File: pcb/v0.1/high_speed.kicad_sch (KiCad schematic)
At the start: 14 parts, among them J4 USB_C_Receptacle_fw, J5 USB_C_Receptacle_fw, J6 690-019-298-412, J7 Conn_01x22_Female, U2 AP22653W6, U3 RT9742SNGV

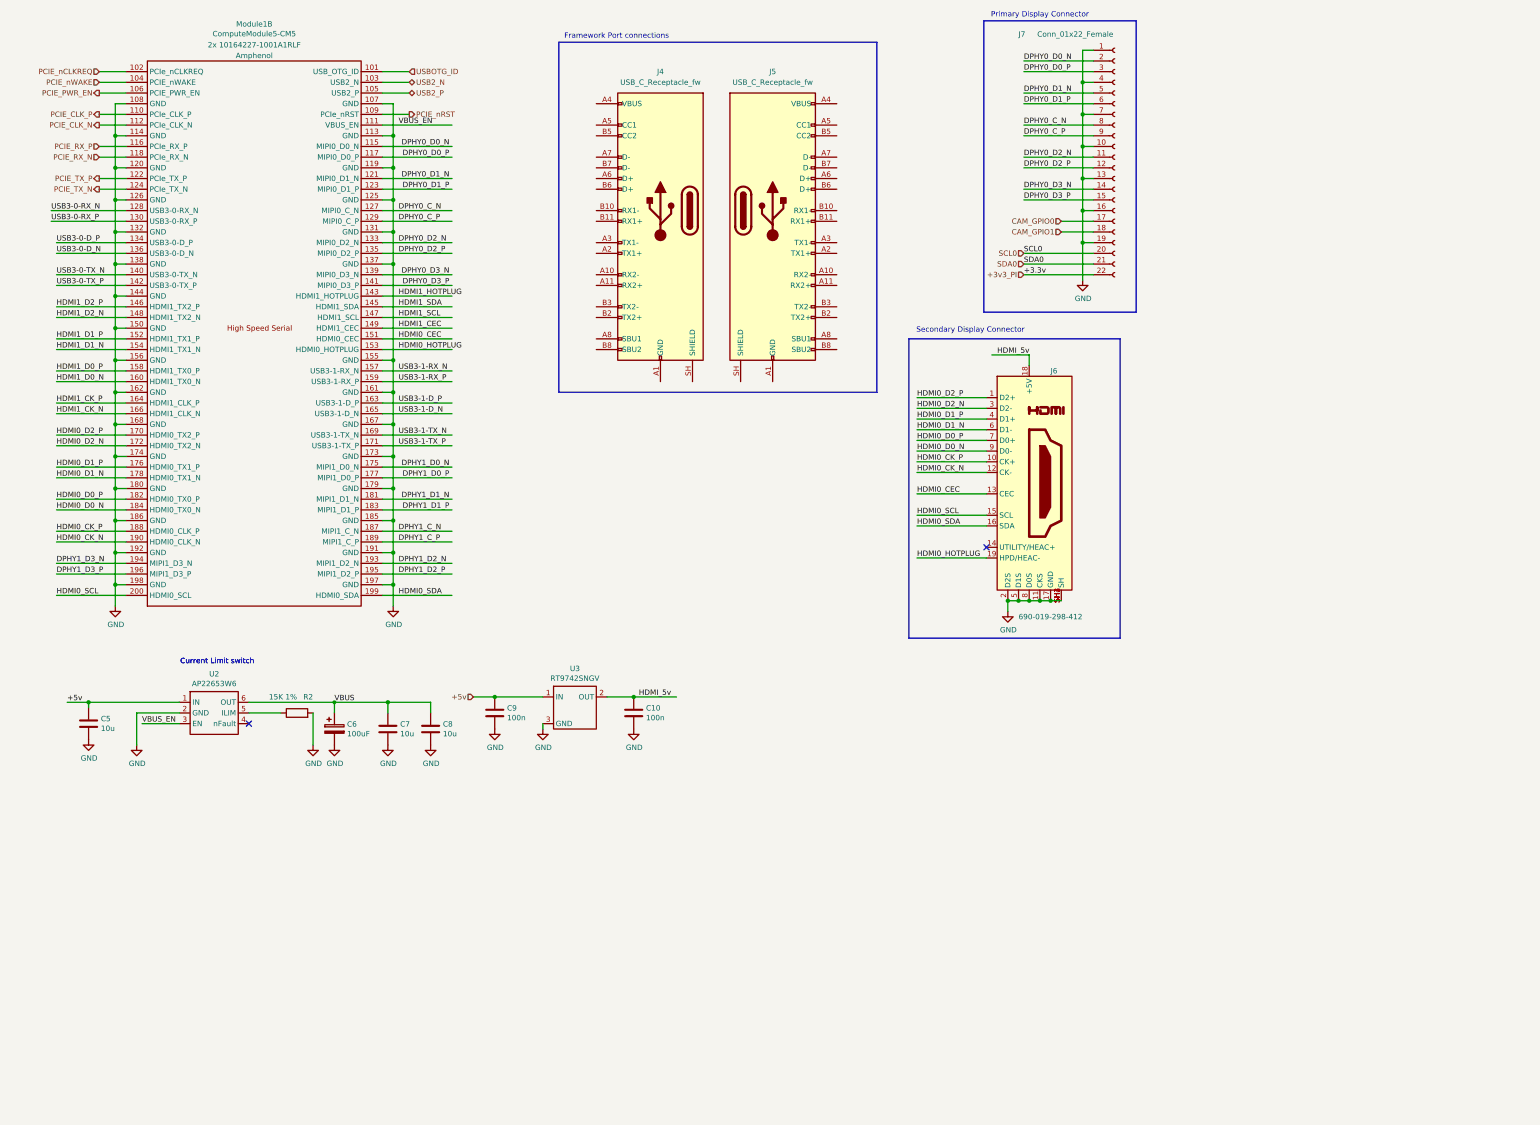
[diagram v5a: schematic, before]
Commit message: Base setup for FW usb ports
The USB system is not complete yet, but all of the basics are done. The
current limit switch, its capacitors, and usb connector parts are
sorted.

However, the current limit, CC pins and second port are not configured
yet.
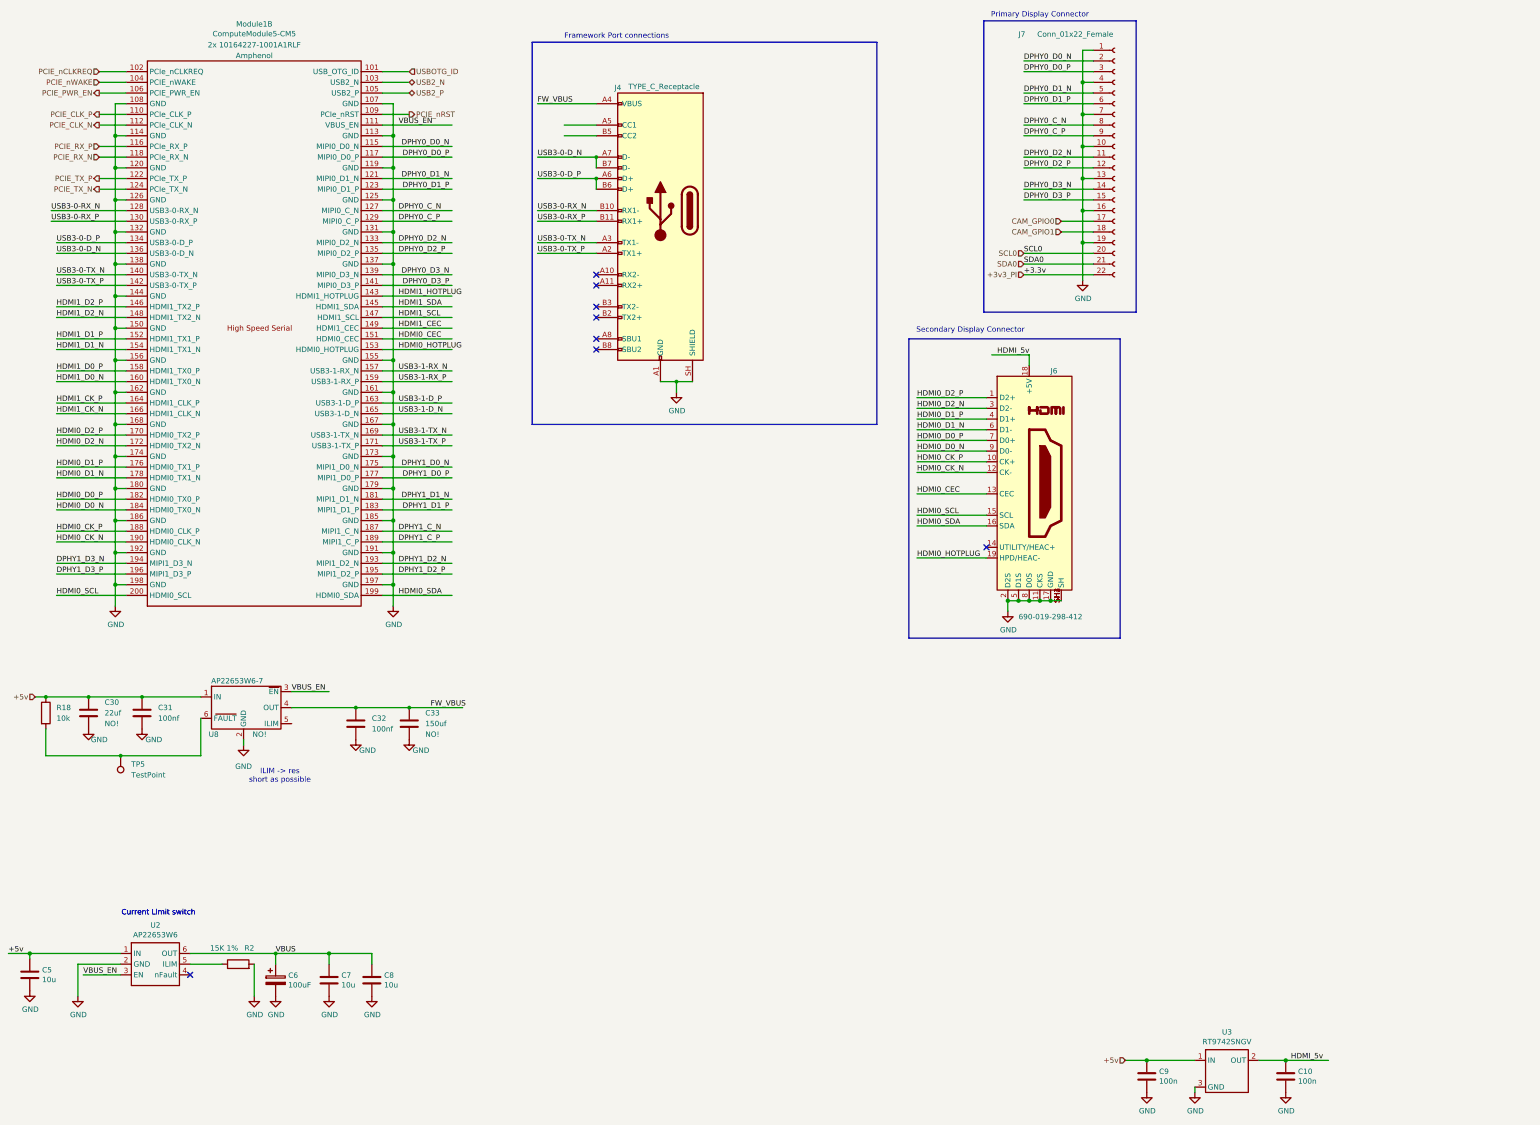
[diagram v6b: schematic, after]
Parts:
- removed J4, J5: USB_C_Receptacle_fw, symbol TH-1-CC:USB_C_Receptacle_fw
- added C30: 22uf, symbol TH-1-CC:C_22uf_AP
- added C31, C32: 100nf, Capacitor_SMD:C_0603_1608Metric, symbol TH-1-CC:C_100nf
- added C33: 150uf, symbol TH-1-CC:C_150uf_AP
- added J4: TYPE_C_Receptacle, symbol TH-1-CC:TYPE_C_Receptacle
- added R18: 10k, Resistor_SMD:R_0603_1608Metric, symbol TH-1-CC:R_10k
- added TP5: TestPoint, symbol Connector:TestPoint
- added U8: AP22653W6-7, symbol TH-1-CC:AP22653W6-7
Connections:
- net +5v: now also C30.1, C31.1, R18.1, U8.1 (IN)
- net GND: now also C30.2, C31.2, C32.2, C33.2, J4.A1 (GND), J4.A12 (GND), J4.B1 (GND), J4.B12 (GND), J4.SH (SHIELD), U8.2 (GND)
- net USB3-0-D_N: now also J4.A7 (D-), J4.B7 (D-)
- net USB3-0-D_P: now also J4.A6 (D+), J4.B6 (D+)
- net USB3-0-RX_N: now also J4.B10 (RX1-)
- net USB3-0-RX_P: now also J4.B11 (RX1+)
- net USB3-0-TX_N: now also J4.A3 (TX1-)
- net USB3-0-TX_P: now also J4.A2 (TX1+)
- net VBUS_EN: now also U8.3 (EN)
- new net: R18.2, TP5.1, U8.6 (FAULT)
- new net FW_VBUS: C32.1, C33.1, J4.A4 (VBUS), J4.A9 (VBUS), J4.B4 (VBUS), J4.B9 (VBUS), U8.4 (OUT)
- no-connect marks 2 -> 8
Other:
- note added: "ILIM -> res short as possible"
- moved on the sheet: C10, C5, C6, C7, C8, C9, R2, U2, U3

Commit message: Finish USB ports!!!
Theoretically both the power input usb type-c port and the two host side
ports are complete. Including a current limit IC that caps the two host
ports at a combined 1.2A.

ESD protection is probably still needed!!!
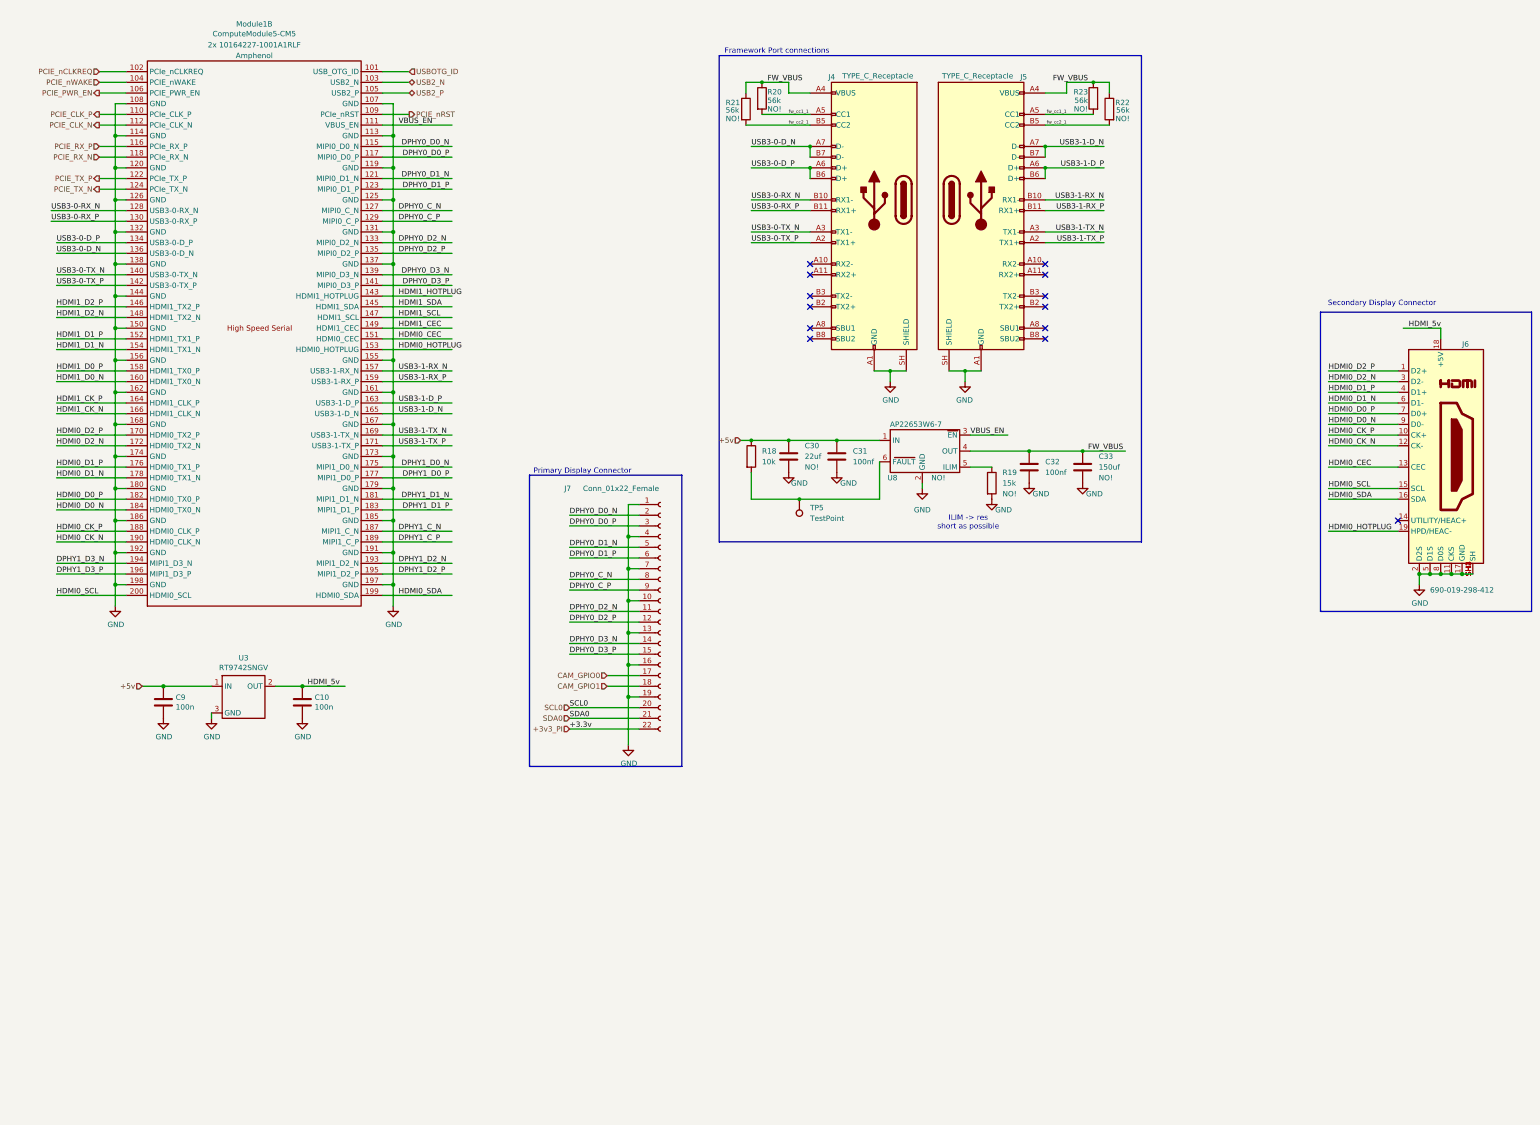
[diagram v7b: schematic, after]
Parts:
- removed C5, C7, C8: 10u, Capacitor_SMD:C_0805_2012Metric, symbol Device:C
- removed C6: 100uF, Capacitor_Tantalum_SMD:CP_EIA-7343-31_Kemet-D, symbol Device:C_Polarized
- removed R2: 15K 1%, Resistor_SMD:R_0402_1005Metric, symbol Device:R
- removed U2: AP22653W6, Package_TO_SOT_SMD:SOT-23-6, symbol CM5IO:AP2553W6
- added J5: TYPE_C_Receptacle, symbol TH-1-CC:TYPE_C_Receptacle
- added R19: 15k, Resistor_SMD:R_0603_1608Metric, symbol TH-1-CC:R_15k
- added R20, R21, R22, R23: 56k, Resistor_SMD:R_0603_1608Metric, symbol TH-1-CC:R_56k
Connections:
- net FW_VBUS: now also J5.A4 (VBUS), J5.A9 (VBUS), J5.B4 (VBUS), J5.B9 (VBUS), R20.1, R21.1, R22.1, R23.1
- net GND: now also J5.A1 (GND), J5.A12 (GND), J5.B1 (GND), J5.B12 (GND), J5.SH (SHIELD), R19.2
- net USB3-1-D_N: now also J5.A7 (D-), J5.B7 (D-)
- net USB3-1-D_P: now also J5.A6 (D+), J5.B6 (D+)
- net USB3-1-RX_N: now also J5.B10 (RX1-)
- net USB3-1-RX_P: now also J5.B11 (RX1+)
- net USB3-1-TX_N: now also J5.A3 (TX1-)
- net USB3-1-TX_P: now also J5.A2 (TX1+)
- net fw_cc1_1: now reaches J4.A5 (CC1)
- net fw_cc1_1: now also J5.A5 (CC1), R20.2, R23.2
- net fw_cc2_1: now reaches J4.B5 (CC2)
- net fw_cc2_1: now also J5.B5 (CC2), R21.2, R22.2
- net at U8.5 (ILIM): now also R19.1
- no-connect marks 8 -> 13
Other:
- note removed: "Current Limit switch"
- moved on the sheet: C10, C30, C31, C32, C33, C9, J4, J6, J7, R18, TP5, U3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

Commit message: Remove the HDMI port
We've decided there is little use to adding an HDMI port on the
prototype if we know that it will not be present on the final board.
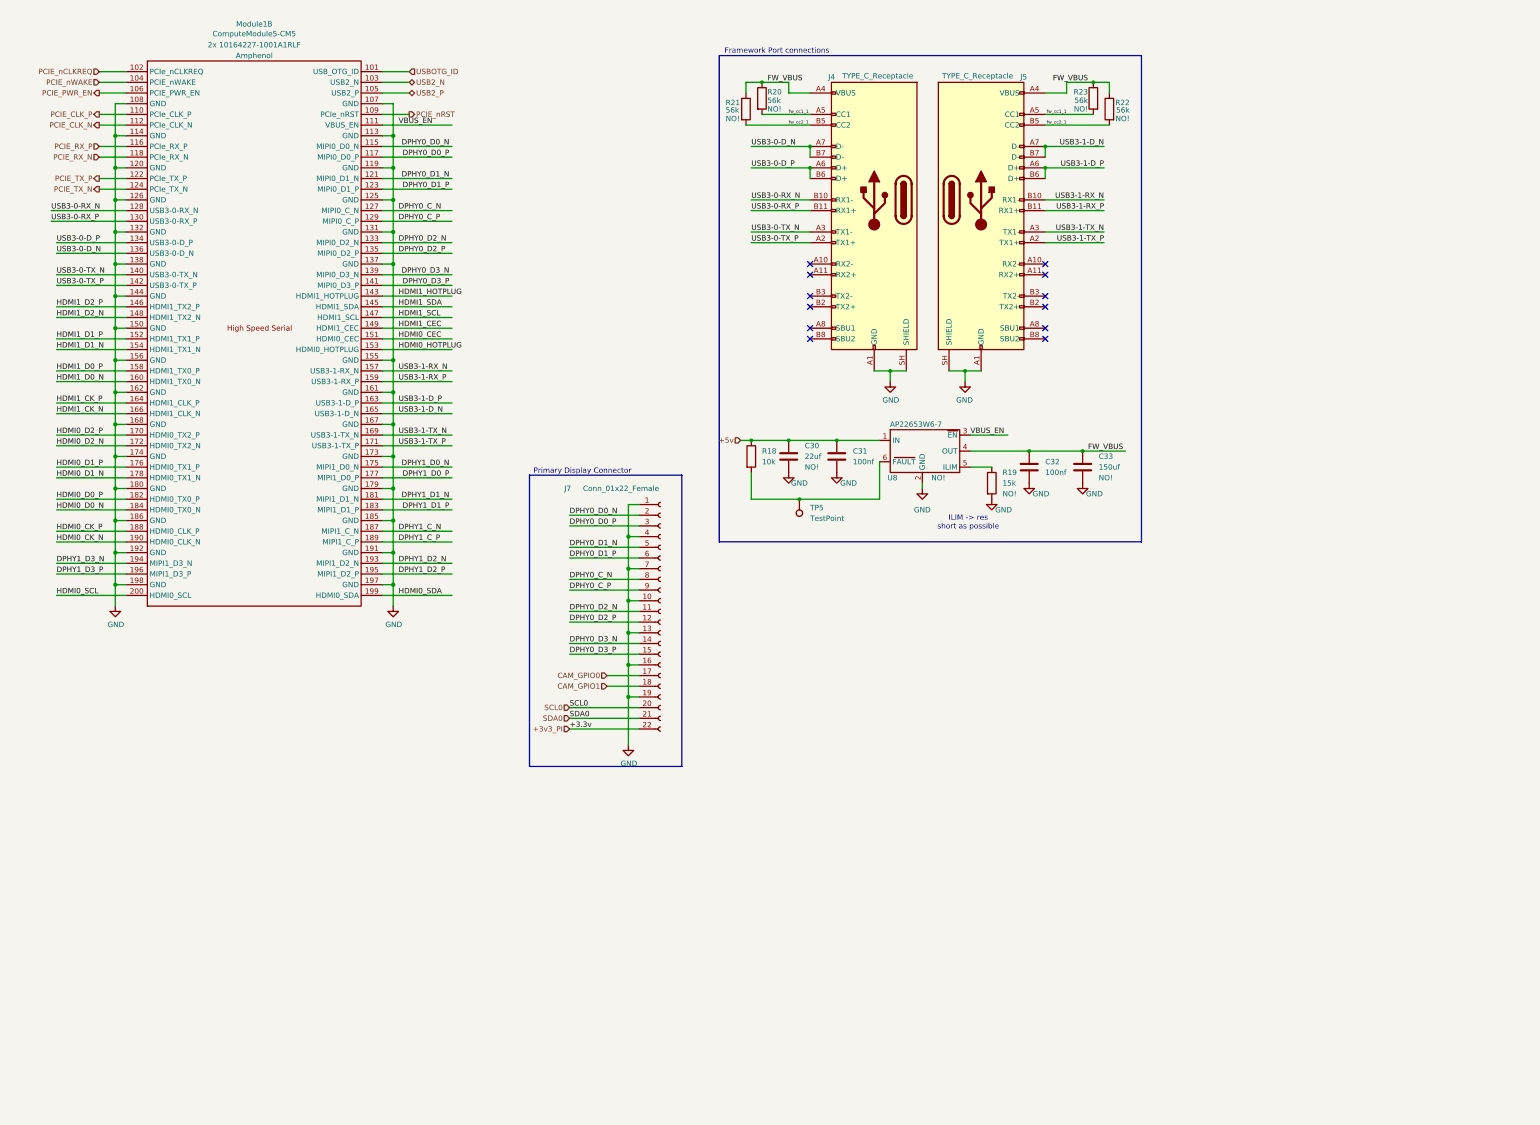
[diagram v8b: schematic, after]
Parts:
- removed C10, C9: 100n, Capacitor_SMD:C_0402_1005Metric, symbol Device:C
- removed J6: 690-019-298-412, CM5IO:EDAC 690-019-298-412, symbol CM5IO:HDMI_A_1.4
- removed U3: RT9742SNGV, Package_TO_SOT_SMD:TSOT-23_HandSoldering, symbol CM5IO:RT9742SNGV
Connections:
- no-connect marks 13 -> 12
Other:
- note removed: "Secondary Display Connector"
